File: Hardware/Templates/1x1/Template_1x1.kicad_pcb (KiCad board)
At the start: 2 copper layers, 42 x 42 mm, 4 parts

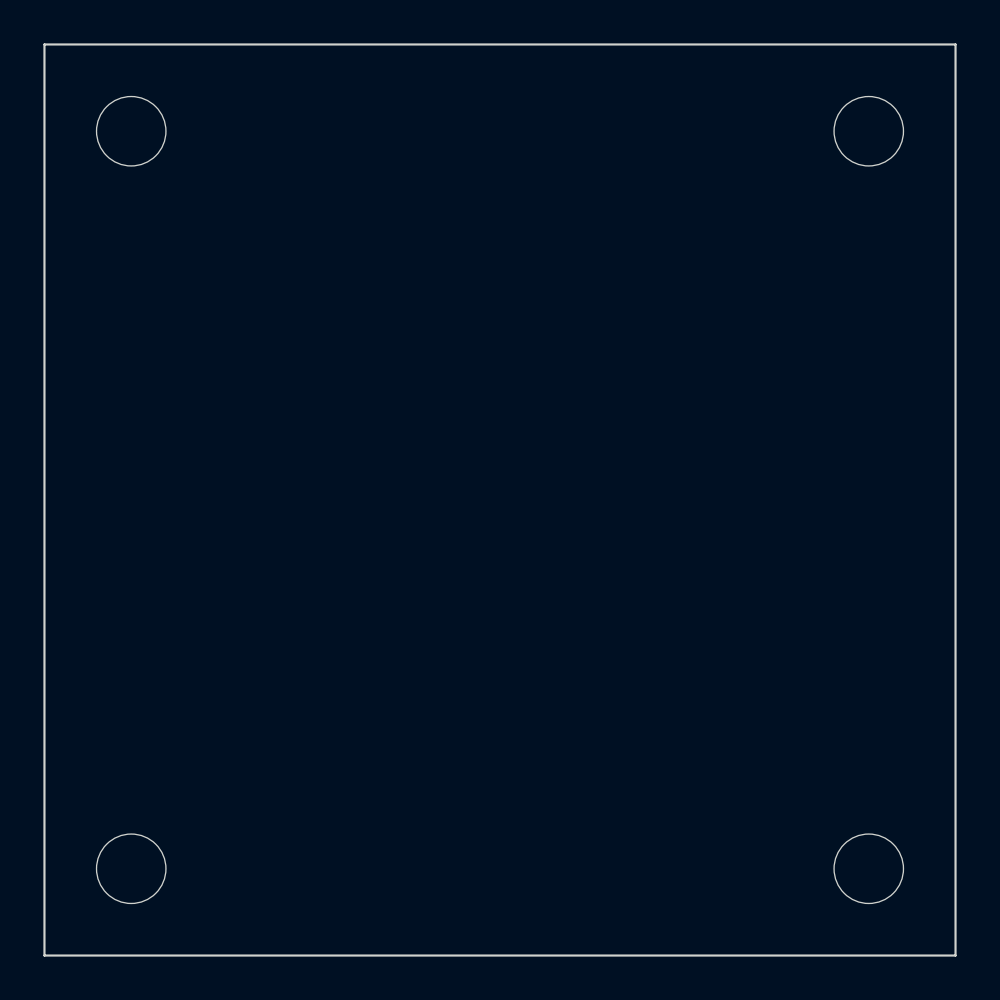
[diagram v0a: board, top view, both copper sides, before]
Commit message: Edited Templates for Hardware
Edited size of templates to fit within containers
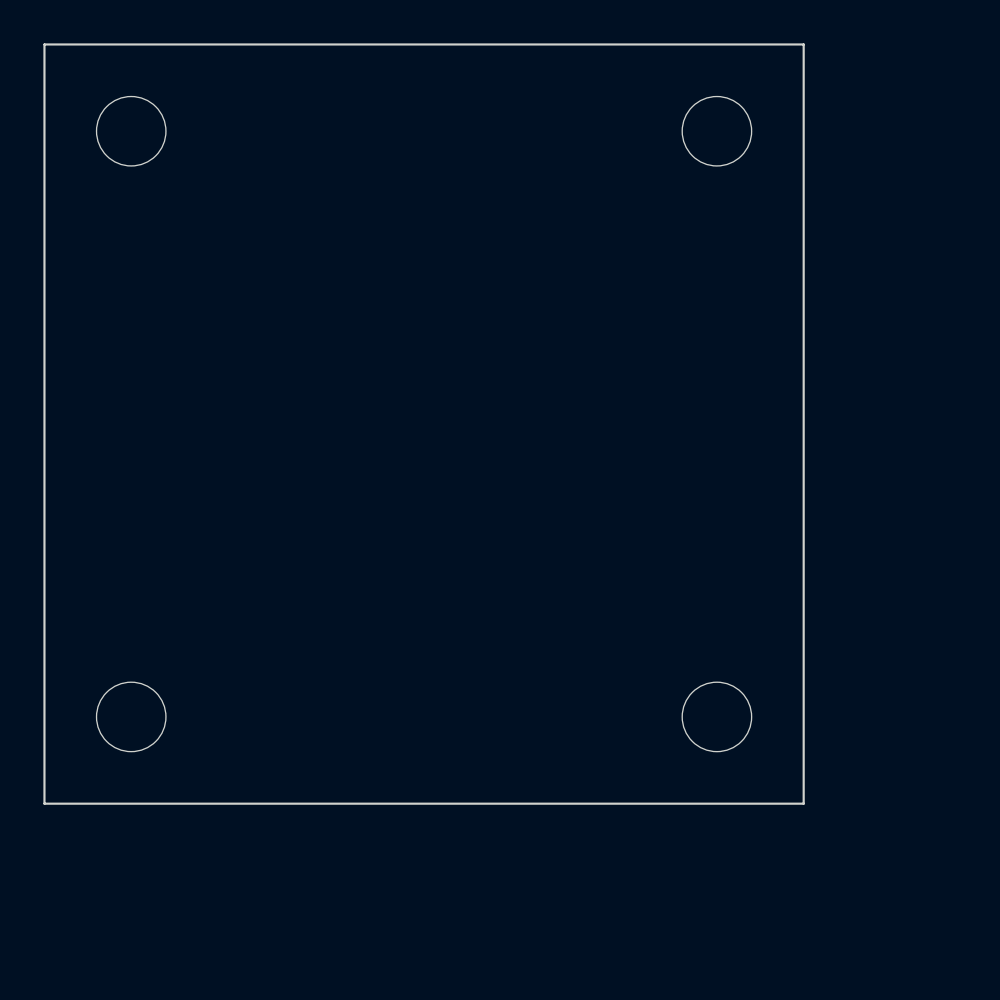
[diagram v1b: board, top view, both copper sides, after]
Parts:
- moved REF** 9.90 mm to (51.0, 51.0)
- moved REF** 7.00 mm to (51.0, 24.0)
- moved REF** 7.00 mm to (24.0, 51.0)
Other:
- board size 42 x 42 mm -> 35 x 35 mm
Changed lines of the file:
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@@
 	(footprint "MountingHole:MountingHole_3.2mm_M3"
 		(layer "F.Cu")
-		(at 58 58)
+		(at 51 51)
 		(descr "Mounting Hole 3.2mm, no annular, M3")
 		(tags "mounting hole 3.2mm no annular m3")
@@
 	(footprint "MountingHole:MountingHole_3.2mm_M3"
 		(layer "F.Cu")
-		(at 58 24)
+		(at 51 24)
 		(descr "Mounting Hole 3.2mm, no annular, M3")
 		(tags "mounting hole 3.2mm no annular m3")
@@
 	(footprint "MountingHole:MountingHole_3.2mm_M3"
 		(layer "F.Cu")
-		(at 24 58)
+		(at 24 51)
 		(descr "Mounting Hole 3.2mm, no annular, M3")
 		(tags "mounting hole 3.2mm no annular m3")
@@
 	(gr_rect
 		(start 20 20)
-		(end 62 62)
+		(end 55 55)
 		(stroke
 			(width 0.1)
